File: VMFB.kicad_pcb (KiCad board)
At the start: 2 copper layers, 141.6 x 109.9 mm, 112 parts, among them J1 Barrel_Jack_Switch, J10 Conn_01x03_Pin, J11 Conn_01x06_Pin, J12 Conn_01x04_Pin, J13 Conn_01x04_Pin, J14 Conn_01x04_Pin, J2 USB_B, J3 Screw_Terminal_01x02, J4 Screw_Terminal_01x03, J5 Conn_01x03_Pin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

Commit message: changed signal LED resistors to 10K from 1K.
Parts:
- R2, R27, R3, R32, R4, R5, R6, R7, R8, R9: value 1K -> 10K
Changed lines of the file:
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@@
         (effects (font (size 1 1) (thickness 0.15)))
     )
-    (fp_text value "1K" (at 1.27 2.37 90) (layer "F.Fab")
+    (fp_text value "10K" (at 1.27 2.37 90) (layer "F.Fab")
         (effects (font (size 1 1) (thickness 0.15)))
     )
@@
         (effects (font (size 1 1) (thickness 0.15)))
     )
-    (fp_text value "1K" (at 1.27 2.37 90) (layer "F.Fab")
+    (fp_text value "10K" (at 1.27 2.37 90) (layer "F.Fab")
         (effects (font (size 1 1) (thickness 0.15)))
     )
@@
         (effects (font (size 1 1) (thickness 0.15)))
     )
-    (fp_text value "1K" (at 1.27 2.37 90) (layer "F.Fab")
+    (fp_text value "10K" (at 1.27 2.37 90) (layer "F.Fab")
         (effects (font (size 1 1) (thickness 0.15)))
     )
@@
         (effects (font (size 1 1) (thickness 0.15)))
     )
-    (fp_text value "1K" (at 1.27 2.37 90) (layer "F.Fab")
+    (fp_text value "10K" (at 1.27 2.37 90) (layer "F.Fab")
         (effects (font (size 1 1) (thickness 0.15)))
     )
@@
         (effects (font (size 1 1) (thickness 0.15)))
     )
-    (fp_text value "1K" (at 1.27 2.37 90) (layer "F.Fab")
+    (fp_text value "10K" (at 1.27 2.37 90) (layer "F.Fab")
         (effects (font (size 1 1) (thickness 0.15)))
     )
@@
         (effects (font (size 1 1) (thickness 0.15)))
     )
-    (fp_text value "1K" (at 1.27 2.37 90) (layer "F.Fab")
+    (fp_text value "10K" (at 1.27 2.37 90) (layer "F.Fab")
         (effects (font (size 1 1) (thickness 0.15)))
     )
@@
         (effects (font (size 1 1) (thickness 0.15)))
     )
-    (fp_text value "1K" (at 1.27 2.37 90) (layer "F.Fab")
+    (fp_text value "10K" (at 1.27 2.37 90) (layer "F.Fab")
         (effects (font (size 1 1) (thickness 0.15)))
     )
@@
         (effects (font (size 1 1) (thickness 0.15)))
     )
-    (fp_text value "1K" (at 1.27 2.37 90) (layer "F.Fab")
+    (fp_text value "10K" (at 1.27 2.37 90) (layer "F.Fab")
         (effects (font (size 1 1) (thickness 0.15)))
     )
@@
         (effects (font (size 1 1) (thickness 0.15)))
     )
-    (fp_text value "1K" (at 1.27 2.37 90) (layer "F.Fab")
+    (fp_text value "10K" (at 1.27 2.37 90) (layer "F.Fab")
         (effects (font (size 1 1) (thickness 0.15)))
     )
@@
         (effects (font (size 1 1) (thickness 0.15)))
     )
-    (fp_text value "1K" (at 1.27 2.37 90) (layer "F.Fab")
+    (fp_text value "10K" (at 1.27 2.37 90) (layer "F.Fab")
         (effects (font (size 1 1) (thickness 0.15)))
     )

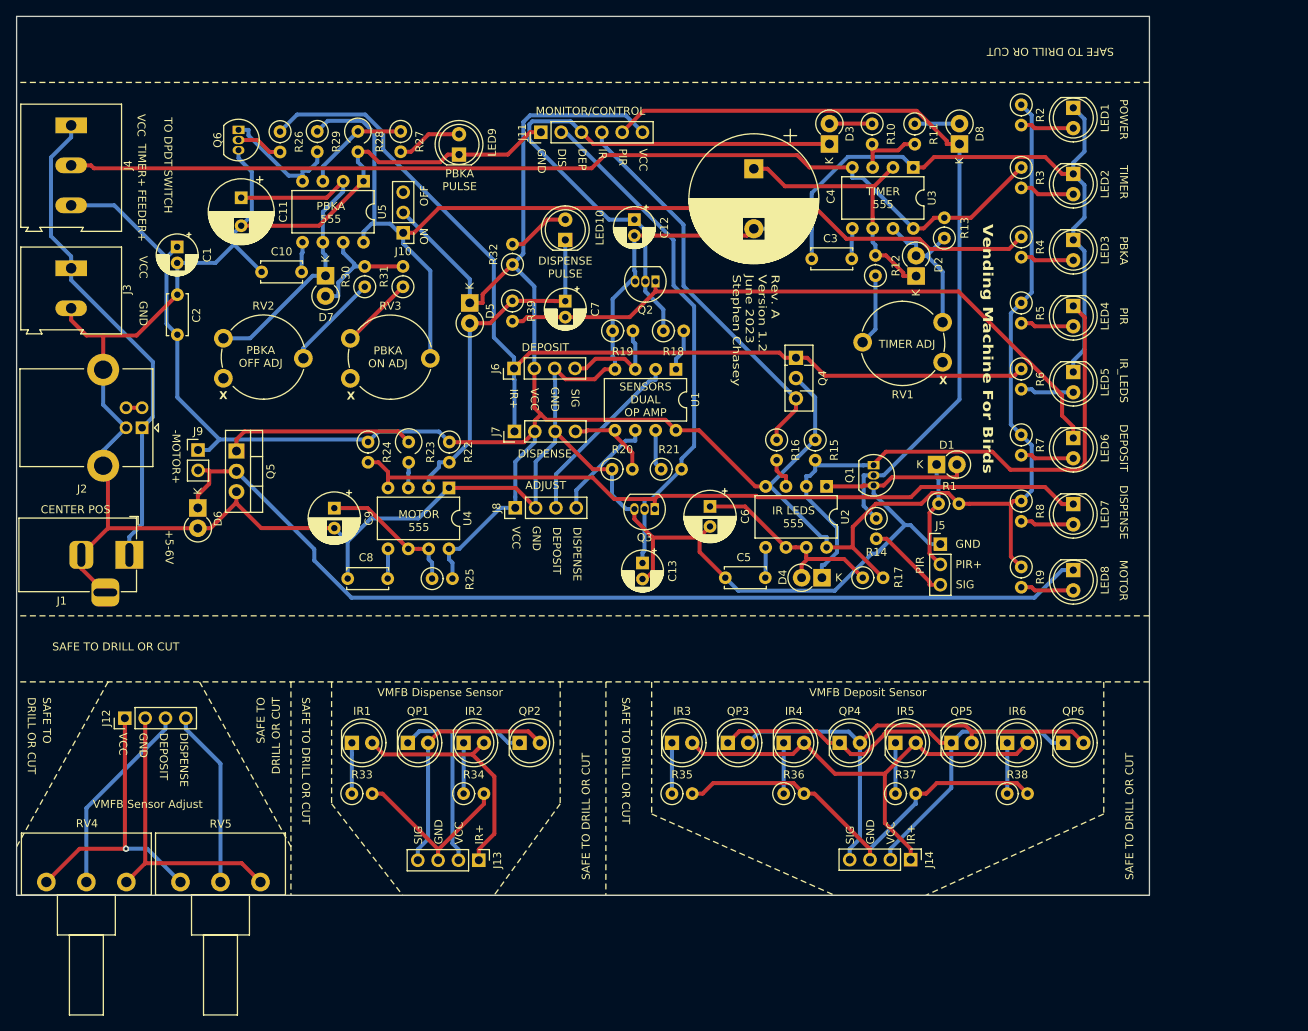
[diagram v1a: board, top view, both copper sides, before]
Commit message: added monitoring-only header, moved IR LED switch transistor from VCC to GND and removed a pin from the sensor headers (no need for separate VCC for the IR LEDS), 100R to 47R on Q$ base, 47R to 22R on Q5 base
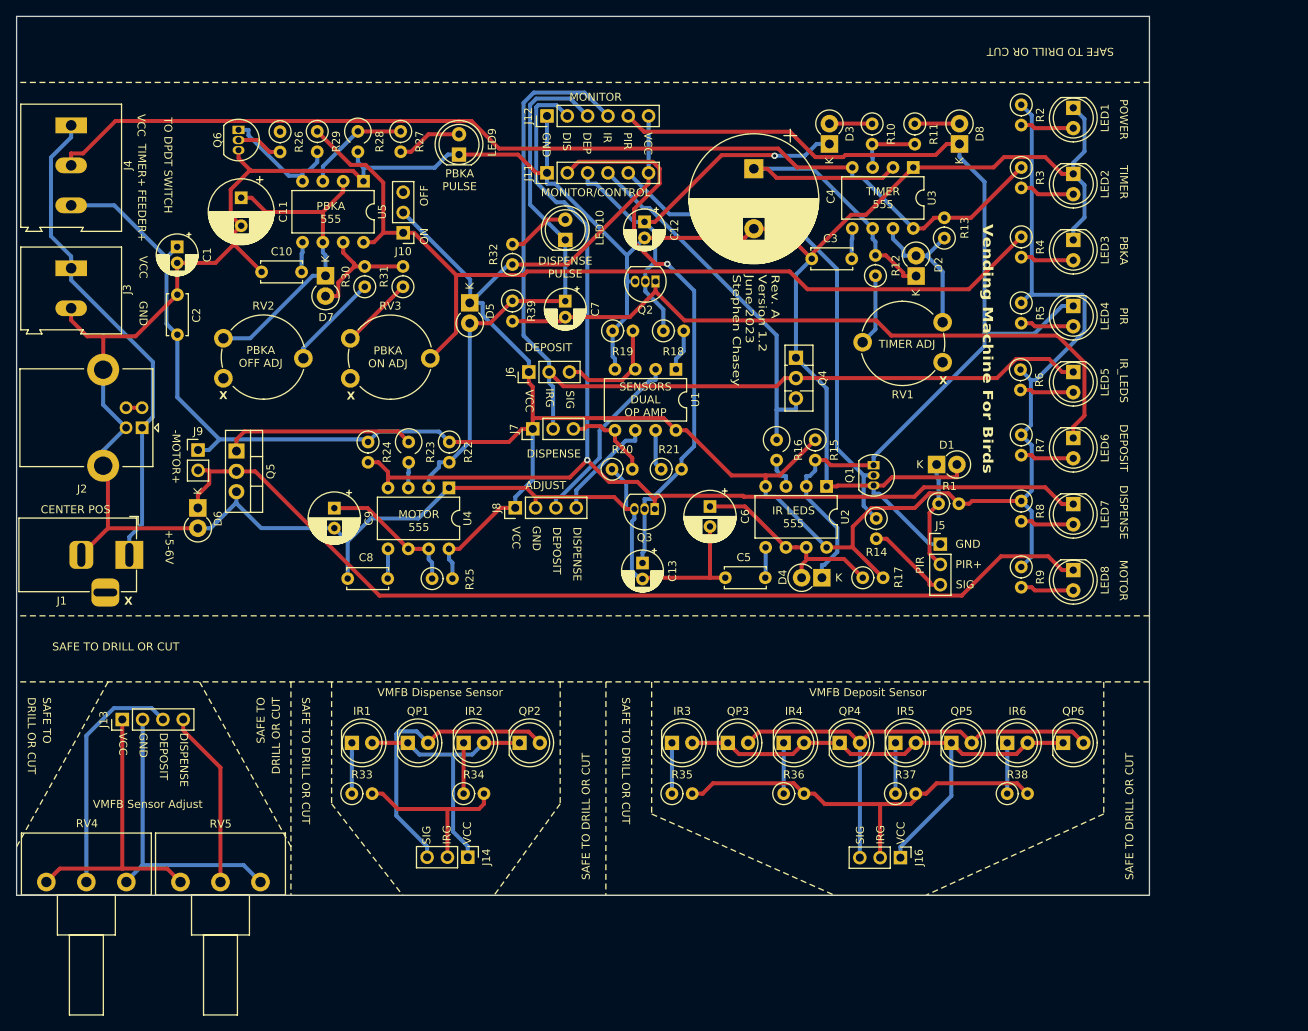
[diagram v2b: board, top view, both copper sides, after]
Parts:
- added J16: Conn_01x03_Pin, Connector_PinHeader_2.54mm:PinHeader_1x03_P2.54mm_Vertical, F.Cu at (181.6, 136.9)
- J12: value Conn_01x04_Pin -> Conn_01x06_Pin; footprint Connector_PinHeader_2.54mm:PinHeader_1x04_P2.54mm_Vertical -> Connector_PinHeader_2.54mm:PinHeader_1x06_P2.54mm_Vertical
- J14, J6, J7: value Conn_01x04_Pin -> Conn_01x03_Pin; footprint Connector_PinHeader_2.54mm:PinHeader_1x04_P2.54mm_Vertical -> Connector_PinHeader_2.54mm:PinHeader_1x03_P2.54mm_Vertical
- R16: value 100R -> 47R; footprint Resistor_THT:R_Axial_DIN0207_L6.3mm_D2.5mm_P2.54mm_Vertical -> Resistor_THT:R_Axial_DIN0309_L9.0mm_D3.2mm_P2.54mm_Vertical
- R23: value 47R -> 22R
- moved J12 91.9 mm to (137.4, 44.2)
- moved J14 55.4 mm to (127.5, 136.8)
- moved J13 47.9 mm to (84.3, 119.6), turned to 90 degrees
- moved J11 5.14 mm to (137.4, 51.3)
- moved J7 2.31 mm to (135.6, 83.3)
- moved J6 1.90 mm to (135.1, 76.2)
- moved C12 1.30 mm to (149.6, 57.4)
- moved R6 0.13 mm to (196.6, 75.9)
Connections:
- net DEPOSIT MON renamed DEPOSIT CON/MON
- net DISPENSE MON renamed DISPENSE CON/MON
- net IR MON renamed IR CON/MON
- D4 pad 1: Net-(D4-K) -> PIR MON
- J1 pad 3: GND -> unconnected-(J1-Pad3)
- J11 pad 5: PIR MON -> PIR CON/MON
- J12 pad 1: Net-(J12-Pin_1) -> GND
- J12 pad 2: Net-(J12-Pin_2) -> MOTOR RESET
- J12 pad 3: Net-(J12-Pin_3) -> MOTOR TRIGGER
- J12 pad 4: Net-(J12-Pin_4) -> IR GND
- J13 pad 1: Net-(IR1-A) -> Net-(J13-Pin_1)
- J14 pad 1: Net-(IR3-A) -> Net-(IR1-A)
- J6 pad 1: IR+ -> VCC
- J6 pad 2: VCC -> IR GND
- J6 pad 3: GND -> DEPOSIT
- J7 pad 1: IR+ -> VCC
- J7 pad 2: VCC -> IR GND
- J7 pad 3: GND -> DISPENSE
- LED4 pad 1: Net-(D4-K) -> PIR MON
- LED5 pad 1: GND -> IR GND
- Q1 pad 1: Net-(D4-K) -> PIR MON
- Q1 pad 2: PIR MON -> PIR CON/MON
- Q4 pad 1: IR+ -> GND
- Q4 pad 2: VCC -> IR GND
- QP1 pad 1: Net-(J13-Pin_2) -> Net-(IR1-A)
- QP1 pad 2: Net-(J13-Pin_4) -> Net-(J14-Pin_3)
- QP2 pad 1: Net-(J13-Pin_2) -> Net-(IR1-A)
- QP2 pad 2: Net-(J13-Pin_4) -> Net-(J14-Pin_3)
- QP3 pad 1: Net-(J14-Pin_2) -> Net-(IR3-A)
- QP3 pad 2: Net-(J14-Pin_4) -> Net-(J16-Pin_3)
- QP4 pad 1: Net-(J14-Pin_2) -> Net-(IR3-A)
- QP4 pad 2: Net-(J14-Pin_4) -> Net-(J16-Pin_3)
- QP5 pad 1: Net-(J14-Pin_2) -> Net-(IR3-A)
- QP5 pad 2: Net-(J14-Pin_4) -> Net-(J16-Pin_3)
- QP6 pad 1: Net-(J14-Pin_2) -> Net-(IR3-A)
- QP6 pad 2: Net-(J14-Pin_4) -> Net-(J16-Pin_3)
- R14 pad 1: PIR MON -> PIR CON/MON
- R15 pad 2: Net-(D4-K) -> PIR MON
- R33 pad 2: Net-(J13-Pin_3) -> Net-(J14-Pin_2)
- R34 pad 2: Net-(J13-Pin_3) -> Net-(J14-Pin_2)
- R35 pad 2: Net-(J14-Pin_3) -> Net-(J16-Pin_2)
- R36 pad 2: Net-(J14-Pin_3) -> Net-(J16-Pin_2)
- R37 pad 2: Net-(J14-Pin_3) -> Net-(J16-Pin_2)
- R38 pad 2: Net-(J14-Pin_3) -> Net-(J16-Pin_2)
- R6 pad 1: IR+ -> VCC
- RV4 pad 1: Net-(J12-Pin_1) -> Net-(J13-Pin_1)
- RV4 pad 2: Net-(J12-Pin_3) -> Net-(J13-Pin_3)
- RV4 pad 3: Net-(J12-Pin_2) -> Net-(J13-Pin_2)
- RV5 pad 1: Net-(J12-Pin_1) -> Net-(J13-Pin_1)
- RV5 pad 2: Net-(J12-Pin_4) -> Net-(J13-Pin_4)
- RV5 pad 3: Net-(J12-Pin_2) -> Net-(J13-Pin_2)
- U2 pad 2: Net-(D4-K) -> PIR MON
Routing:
- net IR+: track 124.6 -> 0.00 mm
- net IR GND: track 0.00 -> 122.9 mm
- net Net-(D4-K): track 74.0 -> 0.00 mm
- net PIR CON/MON: track 0.00 -> 65.5 mm
- net Net-(J14-Pin_4): track 61.4 -> 0.00 mm
- net Net-(J16-Pin_3): track 0.00 -> 59.8 mm
- net MOTOR RESET: track 94.7 -> 148.3 mm, vias 0 -> 1
- net Net-(J16-Pin_2): track 0.00 -> 52.5 mm
- net Net-(J14-Pin_2): track 64.4 -> 22.3 mm
- net Net-(J12-Pin_2): track 36.8 -> 0.00 mm
- net Net-(J13-Pin_1): track 0.00 -> 36.8 mm
- net Net-(J12-Pin_1): track 36.5 -> 0.00 mm, vias 1 -> 0
- net PIR MON: track 99.1 -> 129.5 mm
- net MOTOR TRIGGER: track 44.2 -> 71.4 mm
- net GND: track 445.3 -> 420.5 mm
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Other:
- board text added: "IRG"
- board text added: "MONITOR"
- board text removed: "IR+"

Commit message: moved dispense monitoring directly to the collector of Q2 so you can tell if it's jammed
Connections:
- C7 pad 2: Net-(LED6-K) -> DEPOSIT MON
- J12 pad 3: MOTOR TRIGGER -> DEPOSIT MON
- LED6 pad 1: Net-(LED6-K) -> DEPOSIT MON
- Q2 pad 1: Net-(LED6-K) -> DEPOSIT MON
- R26 pad 1: IR+ -> IR CON/MON
- R39 pad 2: Net-(LED6-K) -> DEPOSIT MON
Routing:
- net DEPOSIT MON: track 0.00 -> 124.3 mm
- net Net-(LED6-K): track 88.0 -> 0.00 mm
- net IR CON/MON: track 46.4 -> 90.6 mm
- net MOTOR TRIGGER: track 71.4 -> 44.2 mm
- net PIR MON: track 129.5 -> 149.3 mm
- net DISPENSE CON/MON: track 70.2 -> 60.0 mm
- net Net-(D2-K): track 46.2 -> 36.5 mm
- net VCC: track 344.8 -> 352.2 mm
- net IR GND: track 122.9 -> 116.1 mm, vias 0 -> 1
- net Net-(J10-Pin_1): track 117.7 -> 116.2 mm
- net MOTOR RESET: track 148.3 -> 146.9 mm
- net GND: track 420.5 -> 421.3 mm, vias 0 -> 1
- net TIMER+: track 131.4 -> 132.1 mm

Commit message: updated version to 1.3
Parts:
- Q1, Q2, Q3, Q6: footprint Package_TO_SOT_THT:TO-92_Inline -> Package_TO_SOT_THT:TO-92_Inline_Wide
- moved Q1 1.77 mm to (178.6, 86.1)
- moved Q3 1.32 mm to (152.1, 93.0)
- moved Q2 1.29 mm to (152.1, 65.4)
- moved Q6 0.83 mm to (98.4, 45.2)
- moved C12 0.79 mm to (149.6, 58.2)
- moved C13 0.57 mm to (149.6, 99.6)
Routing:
- net PIR MON: track 149.3 -> 127.2 mm
- net VCC: track 352.2 -> 339.8 mm
- net Net-(D2-K): track 36.5 -> 47.3 mm
- net IR GND: track 116.1 -> 122.9 mm, vias 1 -> 0
- net GND: track 421.3 -> 419.2 mm, vias 1 -> 0
- net DEPOSIT MON: track 124.3 -> 126.2 mm
- net MOTOR RESET: track 146.9 -> 148.6 mm
- net IR CON/MON: track 90.6 -> 89.2 mm
- net Net-(J10-Pin_1): track 116.2 -> 117.6 mm
- net DISPENSE CON/MON: track 60.0 -> 60.6 mm, vias 1 -> 0
- net Net-(Q6-C): track 15.7 -> 16.2 mm
- net Net-(D6-K): track 123.3 -> 123.9 mm
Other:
- board text added: "Rev. A Version 1.3 July 2023 Stephen Chasey"
- board text removed: "Rev. A Version 1.2 June 2023 Stephen Chasey"

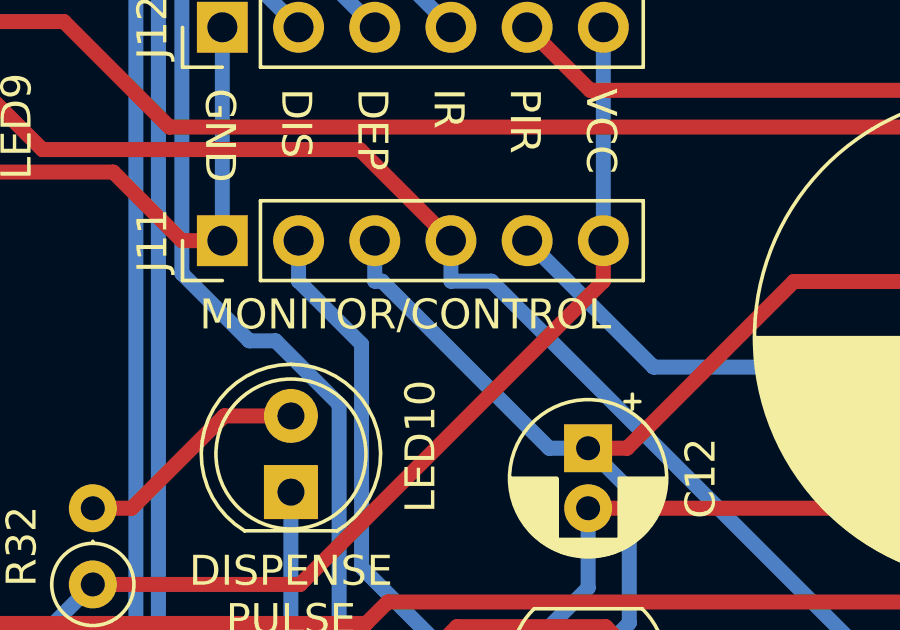
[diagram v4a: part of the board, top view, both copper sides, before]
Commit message: updated control header label and changed footprint for BC547 two commits ago
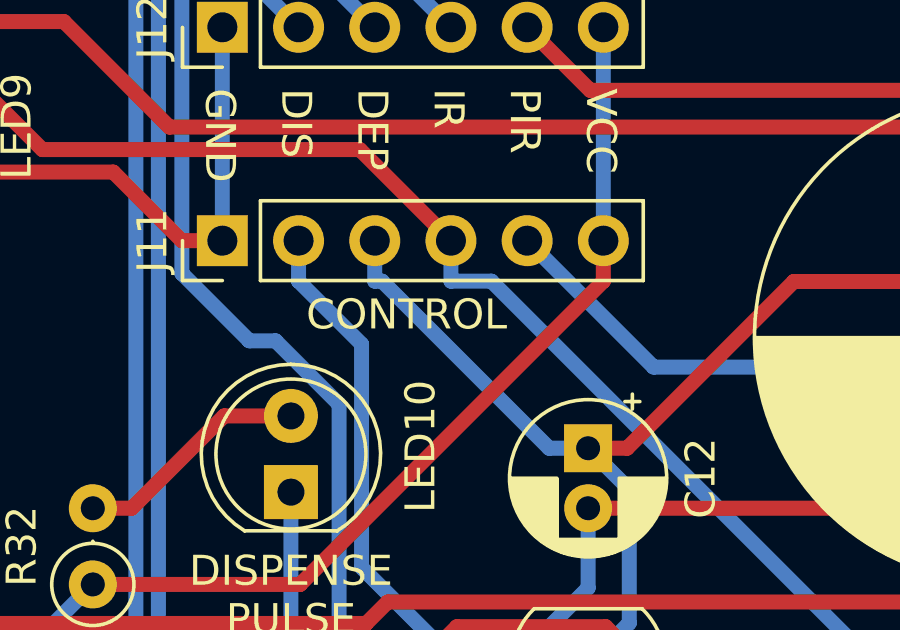
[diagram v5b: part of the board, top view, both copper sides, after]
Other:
- board text added: "CONTROL"
- board text removed: "MONITOR/CONTROL"
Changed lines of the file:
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@@
     (effects (font (size 1 1) (thickness 0.15)) (justify left bottom))
   )
-  (gr_text "MONITOR/CONTROL" (at 136.652 54.356) (layer "F.SilkS")
+  (gr_text "CONTROL" (at 140.208 54.356) (layer "F.SilkS")
     (effects (font (size 1 1) (thickness 0.15)) (justify left bottom))
   )
